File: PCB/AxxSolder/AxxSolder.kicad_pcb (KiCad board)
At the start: 2 copper layers, 39 x 71 mm, 91 parts, among them IC1 LTC4440AHMS8E-5#PBF, IC2 STM32G431KBT6, IC3 TMP236AQDBZRQ1, IC4 OPA2333AIDRBR, IC5 STM32G431KBT6, IC6 TPS54302DDCR, J1 Conn_01x07_Male, J4 Conn_01x07_Male, Q2 2N7002NXAKR, U1 PEC11L-4220F-S0015, U2 BSC014N04LS

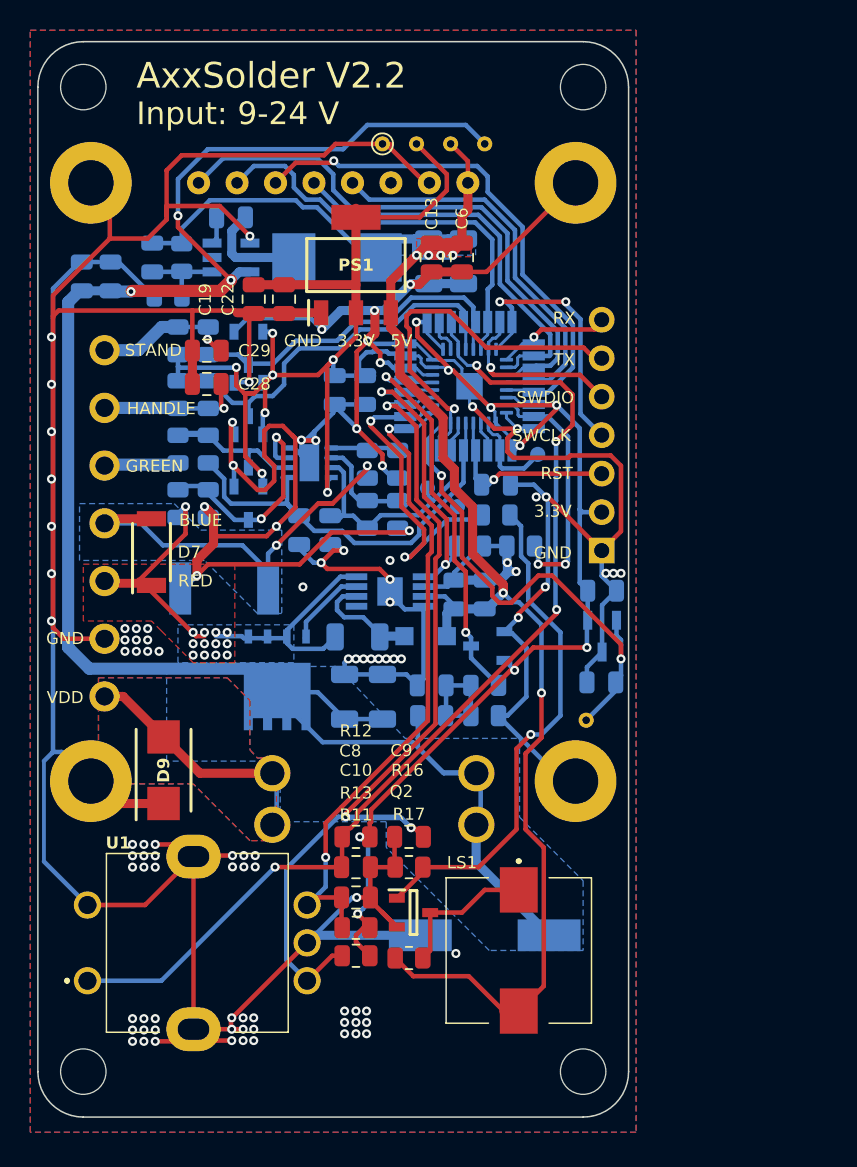
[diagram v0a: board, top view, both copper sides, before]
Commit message: add libraries and import components for USB firmware upload and USB PD
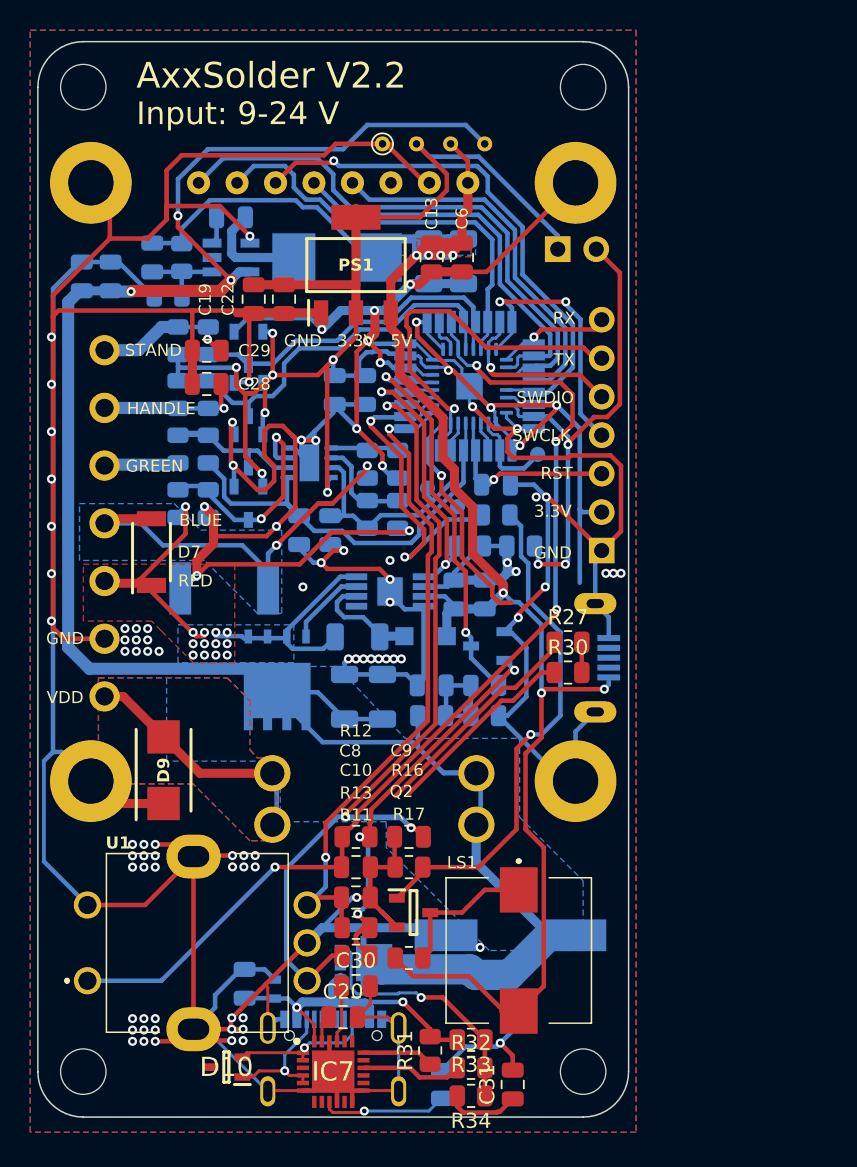
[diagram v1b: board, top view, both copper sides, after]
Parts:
- removed IC3: TMP236AQDBZRQ1, TMP236AQDBZRQ1:SOT95P237X112-3N
- removed TP1: AmbTemp_TP, TestPoint:TestPoint_THTPad_D1.0mm_Drill0.5mm
- added C30: 1u, Capacitor_SMD:C_0805_2012Metric, F.Cu at (118.0, 109.3)
- added C31: 100n, Capacitor_SMD:C_0805_2012Metric, F.Cu at (128.3, 115.8)
- added D10: ESDA25W, ESDA25W:SOT65P210X110-3N, F.Cu at (109.5, 114.7)
- added D8: ESDA25P35-1U1M, ESDA25P35-1U1M:ESDA25P351U1M, B.Cu at (112.7, 109.5)
- added IC7: STUSB4500QTR, STUSB4500QTR:QFN50P400X400X100-25N-D, F.Cu at (116.5, 115.0)
- added J2: USB_B_Micro, USB3140-30-0230-1-C_REVE1:GCT_USB3140-30-0230-1-C_REVE1, B.Cu at (133.4, 87.7)
- added J3: Conn_01x02_Pin, Connector_PinHeader_2.54mm:PinHeader_1x02_P2.54mm_Vertical, B.Cu at (131.3, 60.7)
- added J5: USB4105-GF-A-120, USB4105-GF-A:GCT_USB4105-GF-A-120, B.Cu at (116.5, 116.3)
- added Q1: STL9P3LLH6, STL9P3LLH6:STL20N6F7, B.Cu at (118.5, 107.8)
- added R27: 4k7, Resistor_SMD:R_0805_2012Metric, F.Cu at (132.0, 86.7)
- added R30: 4k7, Resistor_SMD:R_0805_2012Metric, F.Cu at (132.0, 88.7)
- added R31: 1k, Resistor_SMD:R_0805_2012Metric, F.Cu at (122.9, 113.6)
- added R32: 22k, Resistor_SMD:R_0805_2012Metric, F.Cu at (125.6, 114.8)
- added R33: 100k, Resistor_SMD:R_0805_2012Metric, F.Cu at (125.6, 112.9)
- added R34: 22k, Resistor_SMD:R_0805_2012Metric, F.Cu at (125.6, 116.6)
- added R35: 1k, Resistor_SMD:R_0805_2012Metric, B.Cu at (123.7, 115.8)
- C20: value 100n -> 1u; moved to F.Cu
- C4: value 22u -> 22u/16V
- C5: value 100n -> 10u
- moved C5 35.1 mm to (110.7, 109.2), turned to -90 degrees
- moved C20 27.9 mm to (117.2, 111.4), turned to 0 degrees
- moved C23 1.70 mm to (128.2, 106.0)
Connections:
- C20 pad 1: /Ambient_temp -> Net-(IC7-VREG_2V7)
- C5 pad 1: +3.3V -> GND
- C5 pad 2: GND -> /VBUS
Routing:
- net GND: track 451.4 -> 500.6 mm, vias 103 -> 91
- net VDD: track 122.6 -> 149.0 mm, vias 3 -> 4
- net /VBUS: track 0.00 -> 24.0 mm, vias 0 -> 2
- net /Ambient_temp: track 33.6 -> 15.1 mm, vias 2 -> 1
- net /USB_PD_GATE: track 0.00 -> 17.2 mm, vias 0 -> 1
- net Net-(IC2-PB8-BOOT0): track 16.7 -> 32.2 mm, vias 2 -> 3
- net /SCL: track 0.00 -> 14.9 mm
- net /SDA: track 0.00 -> 12.9 mm
- net Net-(D10-CATHODE_2): track 0.00 -> 9.50 mm, vias 0 -> 1
- net Net-(D10-CATHODE_1): track 0.00 -> 8.80 mm, vias 0 -> 1
- net Net-(IC7-DISCH): track 0.00 -> 8.43 mm, vias 0 -> 1
- net Net-(IC7-VBUS_EN_SNK): track 0.00 -> 6.73 mm
- net +5V: track 119.2 -> 124.3 mm, vias 6 -> 7
- net Net-(C31-Pad1): track 0.00 -> 4.90 mm
- net Net-(IC7-VBUS_VS_DISCH): track 0.00 -> 4.72 mm
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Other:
- board text removed: "TMP"

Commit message: update for USB support
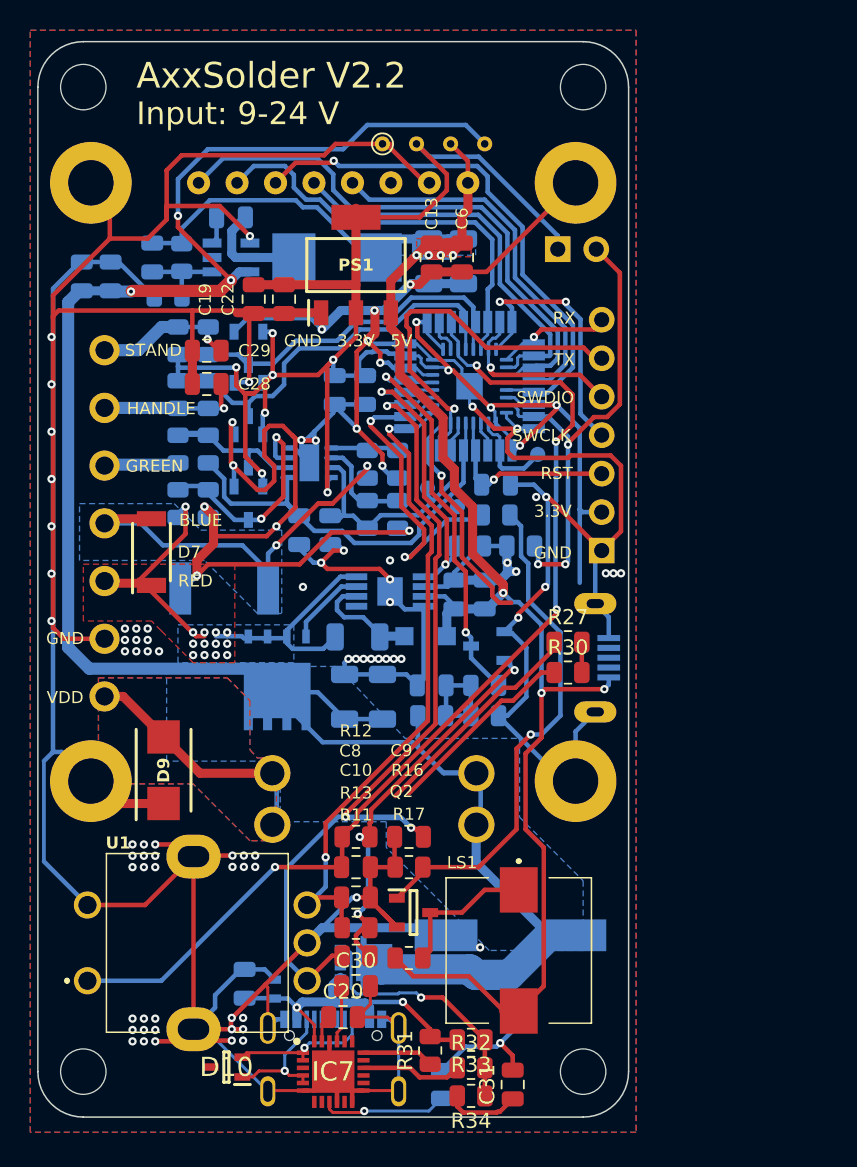
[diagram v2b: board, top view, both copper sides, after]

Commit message: Update to PCB
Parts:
- removed J3: Conn_01x02_Pin, Connector_PinHeader_2.54mm:PinHeader_1x02_P2.54mm_Vertical
- removed J4: Conn_01x07_Male, Connector_PinSocket_2.54mm:PinSocket_1x07_P2.54mm_Vertical
- removed TP2: TestPoint, TestPoint:TestPoint_Pad_D1.0mm
- added D11: 1N5819HW-7-F, 1N5819HW-7-F:SOD3716X145N, F.Cu at (140.6, 65.9)
- added D13: V7NM103-M3_I, V7NM103-M3_I:V7NM103M3I, F.Cu at (141.0, 61.1)
- added IC8: USBLC6-2P6, USBLC6-2P6:USBLC62P6, F.Cu at (146.9, 61.4)
- added J6: Conn_01x06_Socket, Connector_PinSocket_2.54mm:PinSocket_1x06_P2.54mm_Vertical, B.Cu at (134.2, 80.6)
- added S1: PTS636_SM43_SMTR_LFS, PTS636_SM43_SMTR_LFS:PTS636SM43SMTRLFS, B.Cu at (130.8, 61.4)
- moved C7 1.65 mm to (128.9, 76.3)
- moved R15 1.65 mm to (128.9, 78.3), turned to 180 degrees
- moved J2 0.29 mm to (133.2, 87.7)
- moved C5 0.05 mm to (110.6, 109.2)
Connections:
- net /Current renamed /Current_1
- net /Thermocouple renamed /Thermocouple_1
- net Net-(IC2-PA8) renamed /HEATER_2
- net Net-(IC2-PF1-OSC_OUT) renamed /Identification_inp
- D4 pad 6: /SPI_CS -> GND
- IC1 pad 1: /Heater -> /Heater_1
- IC2 pad 10: /Buzzer -> /Thermocouple_2
- IC2 pad 12: /Heater -> /Current_2
- IC2 pad 19: /ENC_Button -> /Handle_inp
- IC2 pad 2: Net-(IC2-PF0-OSC_IN) -> /SPI_DC
- IC2 pad 20: /Handle_inp -> /Stand_inp
- IC2 pad 21: /Stand_inp -> /USB_D-
- IC2 pad 22: /SPI_DC -> /USB_D+
- IC2 pad 25: /MCU_RX -> /SCL
- IC2 pad 29: /SPI_CS -> /ENC_Button
- IC2 pad 30: Net-(IC2-PB7) -> /SDA
- IC2 pad 31: Net-(IC2-PB8-BOOT0) -> /Buzzer
- IC2 pad 8: /Ambient_temp -> /Heater_1
- IC5 pad 10: /Buzzer -> /Thermocouple_2
- IC5 pad 12: /Heater -> /Current_2
- IC5 pad 19: /ENC_Button -> /Handle_inp
- IC5 pad 2: Net-(IC2-PF0-OSC_IN) -> /SPI_DC
- IC5 pad 20: /Handle_inp -> /Stand_inp
- IC5 pad 21: /Stand_inp -> /USB_D-
- IC5 pad 22: /SPI_DC -> /USB_D+
- IC5 pad 25: /MCU_RX -> /SCL
- IC5 pad 29: /SPI_CS -> /ENC_Button
- IC5 pad 30: Net-(IC2-PB7) -> /SDA
- IC5 pad 31: Net-(IC2-PB8-BOOT0) -> /Buzzer
- IC5 pad 8: /Ambient_temp -> /Heater_1
- J2 pad 2: /USB_D- -> Net-(IC8-I/O2_1)
- J2 pad 3: /USB_D+ -> Net-(IC8-I/O1_1)
- Q1 pad 5: VDD -> Net-(D13-A)
- R14 pad 2: Net-(IC2-PB8-BOOT0) -> /Buzzer
- R18 pad 1: /Heater -> /Heater_1
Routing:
- net /SCL: track 14.9 -> 79.3 mm, vias 0 -> 5
- net /SDA: track 12.9 -> 76.3 mm, vias 0 -> 3
- net /USB_D-: track 0.00 -> 41.5 mm, vias 0 -> 4
- net /USB_D+: track 0.00 -> 35.9 mm, vias 0 -> 2
- net /SPI_CS: track 35.1 -> 0.00 mm, vias 1 -> 0
- net Net-(IC2-PB8-BOOT0): track 32.2 -> 0.00 mm, vias 3 -> 0
- net /Heater: track 20.4 -> 0.00 mm, vias 2 -> 0
- net /Ambient_temp: track 15.1 -> 0.00 mm, vias 1 -> 0
- net +3.3V: track 158.3 -> 171.8 mm, vias 15 -> 17
- net /Heater_1: track 0.00 -> 12.7 mm, vias 0 -> 2
- net /Buzzer: track 22.2 -> 32.6 mm
- net GND: track 500.6 -> 490.9 mm, vias 91 -> 87
- net /SPI_DC: track 27.4 -> 36.4 mm, vias 0 -> 2
- net /MCU_RX: track 7.89 -> 0.00 mm, vias 1 -> 0
- net Net-(IC2-PF0-OSC_IN): track 6.13 -> 0.00 mm
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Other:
- board text added: "3.3"
- board text added: "AxxSolder V3.0"
- board text removed: "AxxSolder V2.2"
- board text removed: "RX"
